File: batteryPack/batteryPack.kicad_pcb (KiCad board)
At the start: 2 copper layers, 212.5 x 83 mm, 38 parts, among them J1 Mirco USB, J10 B1+, J11 B1-, J12 B2-, J13 B1+, J14 B1-, J15 B2+, J16 B2-, J2 B1+, J3 B1-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

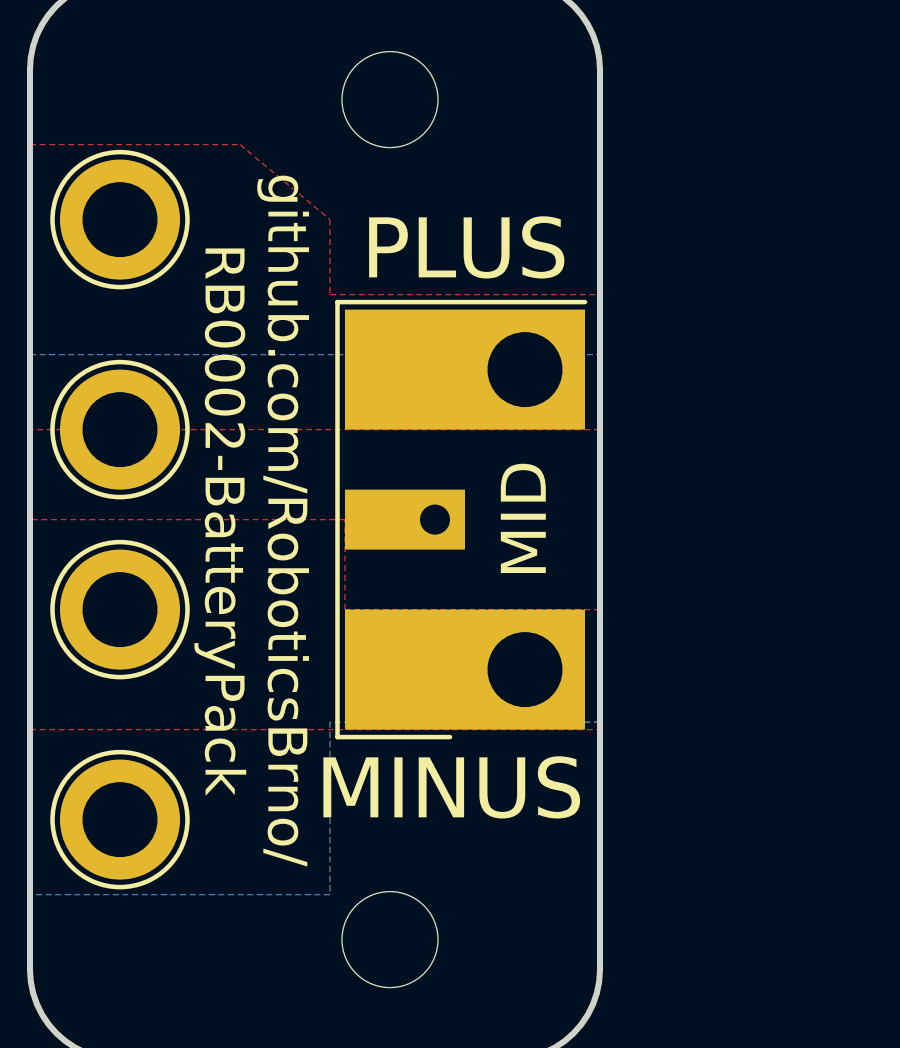
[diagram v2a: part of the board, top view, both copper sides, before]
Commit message: Change connector to screw terminal
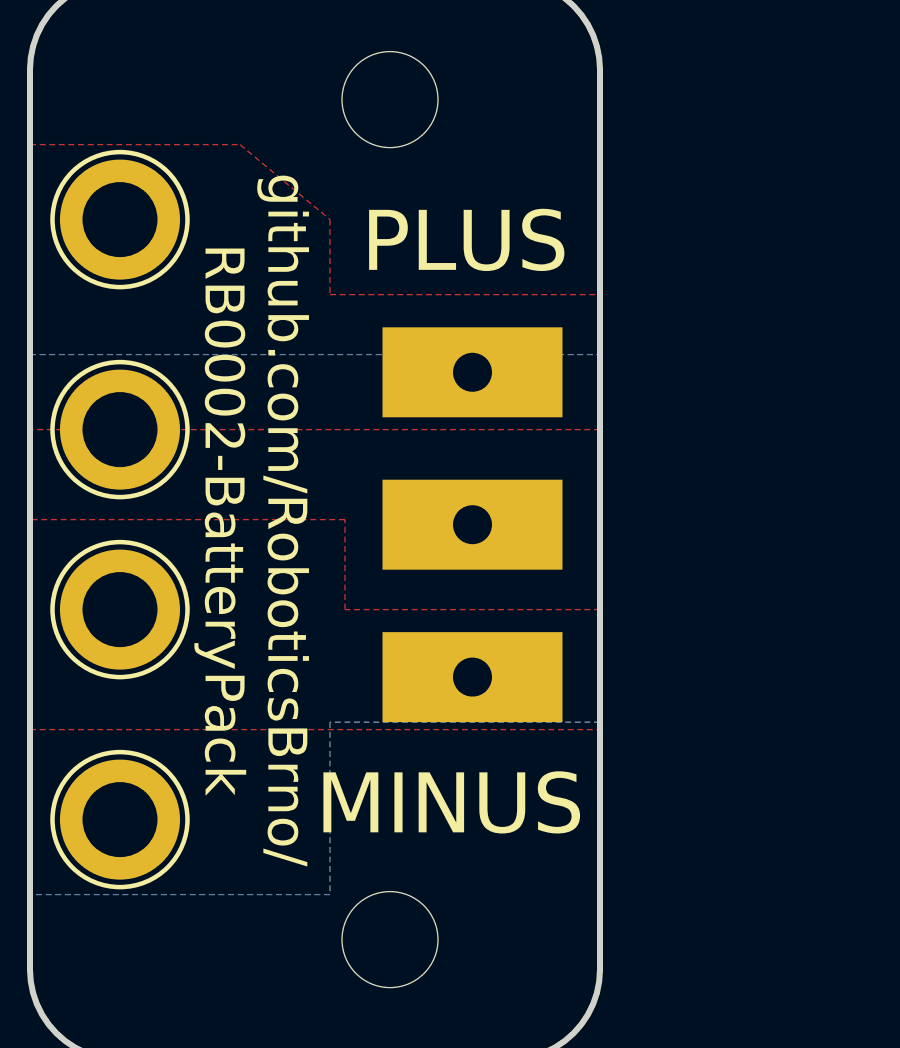
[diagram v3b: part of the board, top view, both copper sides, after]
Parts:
- J6: footprint batteryPack:cableConnector -> batteryPack:Terminal_1x03_P5.08mm_Horizontal
- moved J6 5.53 mm to (131.8, 75.2), turned to 90 degrees
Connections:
- J6 pad 1: /OUT+ -> /OUT-
- J6 pad 3: /OUT- -> /OUT+
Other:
- board text removed: "MID"
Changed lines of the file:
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@@
   (general
     (thickness 1.6)
-    (drawings 131)
+    (drawings 130)
     (tracks 441)
     (zones 0)
@@
   (page A4)
   (layers
-    (0 F.Cu signal hide)
-    (31 B.Cu signal hide)
+    (0 F.Cu signal)
+    (31 B.Cu signal)
     (32 B.Adhes user)
     (33 F.Adhes user)
@@
     (add_net "Net-(D2-Pad2)")
     (add_net "Net-(D3-Pad2)")
+    (add_net "Net-(J1-Pad4)")
     (add_net "Net-(J13-Pad1)")
     (add_net "Net-(J14-Pad1)")
     (add_net "Net-(J15-Pad1)")
     (add_net "Net-(J16-Pad1)")
+    (add_net "Net-(P1-PadA5)")
+    (add_net "Net-(P1-PadA8)")
+    (add_net "Net-(P1-PadB5)")
+    (add_net "Net-(P1-PadB8)")
     (add_net "Net-(R5-Pad1)")
     (add_net "Net-(R6-Pad1)")
     (add_net "Net-(R7-Pad1)")
+    (add_net "Net-(U1-Pad5)")
+    (add_net "Net-(U2-Pad7)")
+    (add_net "Net-(U4-Pad5)")
     (add_net RST)
     (add_net RX)
@@
       (scale (xyz 1 1 1))
       (rotate (xyz -90 0 -90))
+    )
+  )
+  (module batteryPack:Terminal_1x03_P5.08mm_Horizontal (layer F.Cu)
+    (at 131.75 75.25 90)
+    (descr "Terminal Block Phoenix MKDS-3-3-5.08, 3 pins, pitch 5.08mm, size 15.2x11.2mm^2, drill diamater 1.3mm, pad diameter 2.6mm, see http://www.farnell.com/datasheets/2138224.pdf, script-generated using https://github.com/pointhi/kicad-footprint-generator/scripts/TerminalBlock_Phoenix")
+    (tags "THT Terminal Block Phoenix MKDS-3-3-5.08 pitch 5.08mm size 15.2x11.2mm^2 drill 1.3mm pad 2.6mm")
+    (fp_text reference J6 (at 5.08 -6.96 90) (layer F.SilkS) hide
+      (effects (font (size 1 1) (thickness 0.15)))
+    )
+    (fp_text value CableConnector (at 5.08 6.36 90) (layer F.Fab)
+      (effects (font (size 1 1) (thickness 0.15)))
+    )
+    (fp_line (start -2.54 -5.9) (end 12.7 -5.9) (layer F.Fab) (width 0.1))
+    (fp_line (start 12.7 -5.9) (end 12.7 5.3) (layer F.Fab) (width 0.1))
+    (fp_line (start 12.7 5.3) (end -2.04 5.3) (layer F.Fab) (width 0.1))
+    (fp_line (start -2.04 5.3) (end -2.54 4.8) (layer F.Fab) (width 0.1))
+    (fp_line (start -2.54 4.8) (end -2.54 -5.9) (layer F.Fab) (width 0.1))
+    (fp_line (start -2.54 4.8) (end 12.7 4.8) (layer F.Fab) (width 0.1))
+    (fp_line (start -2.54 2.3) (end 12.7 2.3) (layer F.Fab) (width 0.1))
+    (fp_line (start -2.54 -3.9) (end 12.7 -3.9) (layer F.Fab) (width 0.1))
+    (fp_line (start 1.273 -1.517) (end -1.517 1.273) (layer F.Fab) (width 0.1))
+    (fp_line (start -3.04 -6.4) (end -3.04 5.8) (layer F.CrtYd) (width 0.05))
+    (fp_line (start -3.04 5.8) (end 13.21 5.8) (layer F.CrtYd) (width 0.05))
+    (fp_line (start 13.21 5.8) (end 13.21 -6.4) (layer F.CrtYd) (width 0.05))
+    (fp_line (start 13.21 -6.4) (end -3.04 -6.4) (layer F.CrtYd) (width 0.05))
+    (fp_text user %R (at 5.08 3.1 90) (layer F.Fab)
+      (effects (font (size 1 1) (thickness 0.15)))
+    )
+    (pad 1 thru_hole rect (at 0 0 90) (size 3 6) (drill 1.3) (layers *.Cu *.Mask)
+      (net 24 /OUT-))
+    (pad 2 thru_hole rect (at 5.08 0 90) (size 3 6) (drill 1.3) (layers *.Cu *.Mask)
+      (net 23 /MID))
+    (pad 3 thru_hole rect (at 10.16 0 90) (size 3 6) (drill 1.3) (layers *.Cu *.Mask)
+      (net 22 /OUT+))
+    (model ${KISYS3DMOD}/TerminalBlock_Phoenix.3dshapes/TerminalBlock_Phoenix_MKDS-3-3-5.08_1x03_P5.08mm_Horizontal.wrl
+      (at (xyz 0 0 0))
+      (scale (xyz 1 1 1))
+      (rotate (xyz 0 0 0))
     )
   )
@@
       (rotate (xyz 0 0 0))
     )
-  )
-  (module batteryPack:cableConnector (layer F.Cu)
-    (at 133.5 70)
-    (fp_text reference J6 (at 0 -8.5) (layer F.SilkS) hide
-      (effects (font (size 1 1) (thickness 0.15)))
-    )
-    (fp_text value CableConnector (at 0 -11) (layer F.Fab)
-      (effects (font (size 1 1) (thickness 0.15)))
-    )
-    (fp_line (start -6.25 7.25) (end -2.5 7.25) (layer F.SilkS) (width 0.15))
-    (fp_line (start -6.25 -7.25) (end -6.25 7.25) (layer F.SilkS) (width 0.15))
-    (fp_line (start 2 -7.25) (end -6.25 -7.25) (layer F.SilkS) (width 0.15))
-    (pad 2 thru_hole rect (at -3 0) (size 4 2) (drill 1 (offset -1 0)) (layers *.Cu *.Mask)
-      (net 23 /MID))
-    (pad 3 thru_hole rect (at 0 5) (size 8 4) (drill 2.5 (offset -2 0)) (layers *.Cu *.Mask)
-      (net 24 /OUT-))
-    (pad 1 thru_hole rect (at 0 -5) (size 8 4) (drill 2.5 (offset -2 0)) (layers *.Cu *.Mask)
-      (net 22 /OUT+))
   )
   (module batteryPack:2mm_Banana-Vertical (layer F.Cu)
@@
   (gr_arc (start 133 85) (end 133 88) (angle -90) (layer Edge.Cuts) (width 0.2))
   (gr_arc (start 133 55) (end 136 55) (angle -90) (layer Edge.Cuts) (width 0.2))
-  (gr_text MID (at 133.5 70 90) (layer F.SilkS)
-    (effects (font (size 1.5 1.5) (thickness 0.3)))
-  )
-  (gr_text MINUS (at 131 79) (layer F.SilkS)
+  (gr_text MINUS (at 131 79.5) (layer F.SilkS)
     (effects (font (size 2 2) (thickness 0.4)))
   )
-  (gr_text PLUS (at 131.5 61) (layer F.SilkS)
+  (gr_text PLUS (at 131.5 60.75) (layer F.SilkS)
     (effects (font (size 2 2) (thickness 0.4)))
   )

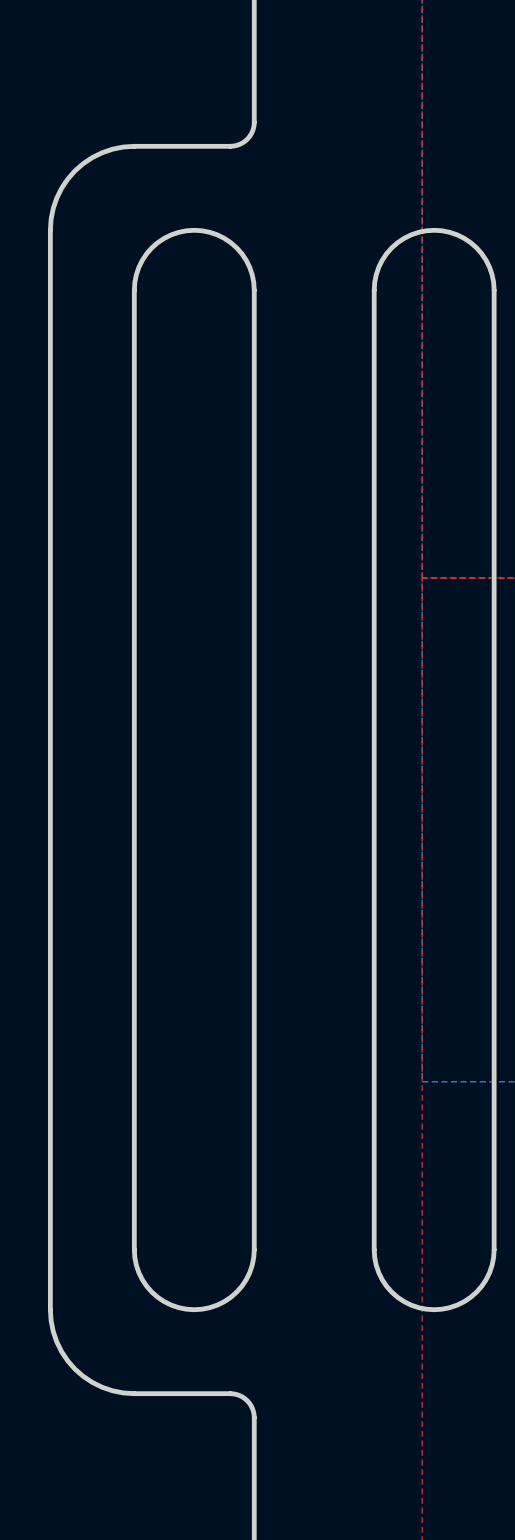
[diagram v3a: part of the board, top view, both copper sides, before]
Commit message: Tune pull handle and battery panel
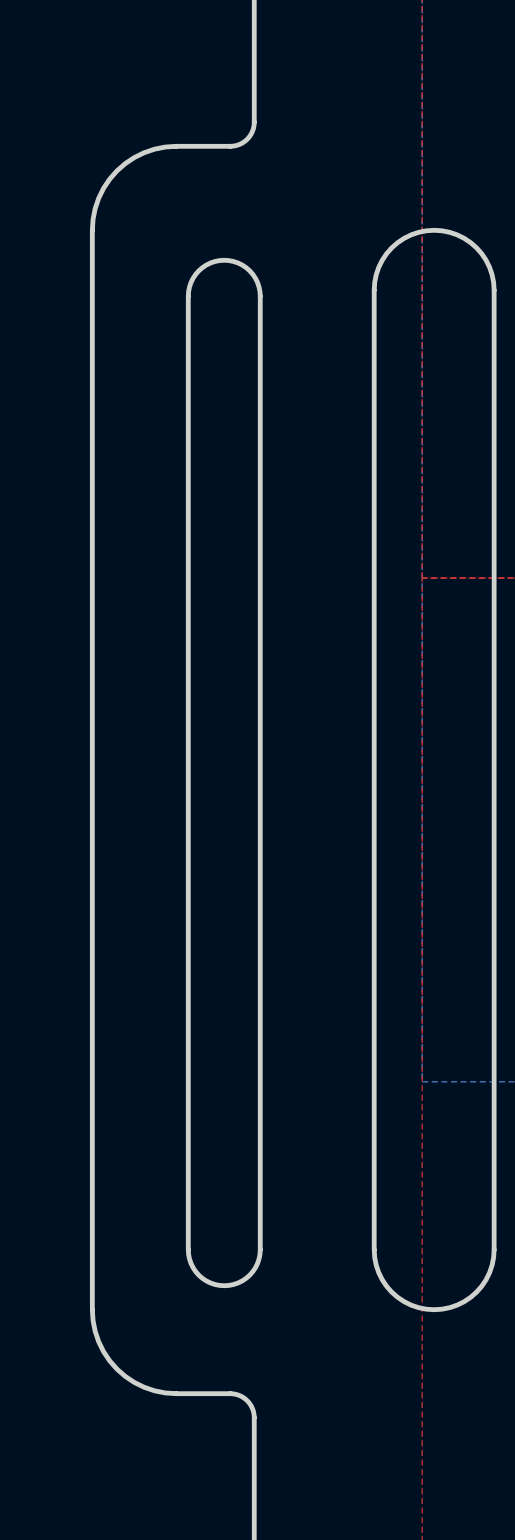
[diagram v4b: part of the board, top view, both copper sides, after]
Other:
- board size 212.5 x 83 mm -> 210.8 x 83 mm
- board text added: "Panel tab position"
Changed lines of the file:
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@@
-(kicad_pcb (version 20171130) (host pcbnew 5.1.5-52549c5~86~ubuntu19.10.1)
+(kicad_pcb (version 20171130) (host pcbnew 5.1.5+dfsg1-2build2)
   (general
     (thickness 1.6)
-    (drawings 130)
+    (drawings 138)
     (tracks 441)
     (zones 0)
@@
     (add_net "Net-(D2-Pad2)")
     (add_net "Net-(D3-Pad2)")
-    (add_net "Net-(J1-Pad4)")
     (add_net "Net-(J13-Pad1)")
     (add_net "Net-(J14-Pad1)")
     (add_net "Net-(J15-Pad1)")
     (add_net "Net-(J16-Pad1)")
-    (add_net "Net-(P1-PadA5)")
-    (add_net "Net-(P1-PadA8)")
-    (add_net "Net-(P1-PadB5)")
-    (add_net "Net-(P1-PadB8)")
     (add_net "Net-(R5-Pad1)")
     (add_net "Net-(R6-Pad1)")
     (add_net "Net-(R7-Pad1)")
-    (add_net "Net-(U1-Pad5)")
-    (add_net "Net-(U2-Pad7)")
-    (add_net "Net-(U4-Pad5)")
     (add_net RST)
     (add_net RX)
@@
   (module batteryPack:BAT_BK-18650-PC4 (layer B.Cu)
     (at 50 70 270)
-    (fp_text reference BT1 (at -36.195 19.05 90) (layer B.SilkS)
+    (fp_text reference BT1 (at -36.195 19.05 90) (layer B.SilkS) hide
       (effects (font (size 1 1) (thickness 0.15)) (justify mirror))
     )
@@
     )
   )
+  (gr_text "Panel tab position" (at 80.5 103) (layer Cmts.User)
+    (effects (font (size 1 1) (thickness 0.15)))
+  )
+  (gr_text "Panel tab position" (at 80.25 86.75) (layer Cmts.User)
+    (effects (font (size 1 1) (thickness 0.15)))
+  )
+  (gr_text "Panel tab position" (at 80.5 53.5) (layer Cmts.User)
+    (effects (font (size 1 1) (thickness 0.15)))
+  )
+  (gr_text "Panel tab position" (at 80.5 37) (layer Cmts.User)
+    (effects (font (size 1 1) (thickness 0.15)))
+  )
+  (gr_line (start 73 37) (end 68.5 37) (layer Cmts.User) (width 0.3))
+  (gr_line (start 73 103) (end 68.5 103) (layer Cmts.User) (width 0.3))
+  (gr_line (start 73 86.75) (end 68.5 86.75) (layer Cmts.User) (width 0.3))
+  (gr_line (start 73 53.5) (end 68.5 53.5) (layer Cmts.User) (width 0.3))
+  (gr_arc (start 28.75 90) (end 27.25 90) (angle -180) (layer Edge.Cuts) (width 0.2))
+  (gr_arc (start 28.75 50.25) (end 30.25 50.25) (angle -180) (layer Edge.Cuts) (width 0.2))
   (gr_line (start 31 109) (end 32.75 109) (layer Edge.Cuts) (width 0.2))
   (gr_line (start 67.25 109) (end 69 109) (layer Edge.Cuts) (width 0.2))
@@
   (gr_arc (start 64.75 29.75) (end 66 29.75) (angle -90) (layer Edge.Cuts) (width 0.2))
   (gr_line (start 64.75 28.5) (end 35.25 28.5) (layer Edge.Cuts) (width 0.2))
-  (gr_line (start 21.5 47.5) (end 21.5 92.5) (layer Edge.Cuts) (width 0.2))
-  (gr_arc (start 25 92.5) (end 21.5 92.5) (angle -90) (layer Edge.Cuts) (width 0.2))
-  (gr_line (start 29 96) (end 25 96) (layer Edge.Cuts) (width 0.2))
-  (gr_arc (start 25 47.5) (end 25 44) (angle -90) (layer Edge.Cuts) (width 0.2))
-  (gr_line (start 29 44) (end 25 44) (layer Edge.Cuts) (width 0.2))
-  (gr_line (start 25 50) (end 25 90) (layer Edge.Cuts) (width 0.2))
-  (gr_arc (start 27.5 50) (end 30 50) (angle -180) (layer Edge.Cuts) (width 0.2))
-  (gr_arc (start 27.5 90) (end 25 90) (angle -180) (layer Edge.Cuts) (width 0.2))
-  (gr_line (start 30 50) (end 30 90) (layer Edge.Cuts) (width 0.2))
+  (gr_line (start 23.25 47.5) (end 23.25 92.5) (layer Edge.Cuts) (width 0.2))
+  (gr_arc (start 26.75 92.5) (end 23.25 92.5) (angle -90) (layer Edge.Cuts) (width 0.2))
+  (gr_line (start 29 96) (end 26.75 96) (layer Edge.Cuts) (width 0.2))
+  (gr_arc (start 26.75 47.5) (end 26.75 44) (angle -90) (layer Edge.Cuts) (width 0.2))
+  (gr_line (start 29 44) (end 26.75 44) (layer Edge.Cuts) (width 0.2))
+  (gr_line (start 27.25 50.25) (end 27.25 90) (layer Edge.Cuts) (width 0.2))
+  (gr_line (start 30.25 50.25) (end 30.25 90) (layer Edge.Cuts) (width 0.2))
   (gr_arc (start 29 97) (end 30 97) (angle -90) (layer Edge.Cuts) (width 0.2))
   (gr_line (start 30 97) (end 30 108) (layer Edge.Cuts) (width 0.2))
@@
   (gr_line (start 122.25 48.75) (end 122.25 90) (layer F.CrtYd) (width 0.15))
   (dimension 40 (width 0.3) (layer F.Fab)
-    (gr_text "40,000 mm" (at 50 118.449999) (layer F.Fab)
-      (effects (font (size 1 1) (thickness 0.15)))
-    )
-    (feature1 (pts (xy 70 108) (xy 70 117.58642)))
-    (feature2 (pts (xy 30 108) (xy 30 117.58642)))
-    (crossbar (pts (xy 30 116.999999) (xy 70 116.999999)))
-    (arrow1a (pts (xy 70 116.999999) (xy 68.873496 117.58642)))
-    (arrow1b (pts (xy 70 116.999999) (xy 68.873496 116.413578)))
-    (arrow2a (pts (xy 30 116.999999) (xy 31.126504 117.58642)))
-    (arrow2b (pts (xy 30 116.999999) (xy 31.126504 116.413578)))
+    (gr_text "40,000 mm" (at 50 121.2) (layer F.Fab)
+      (effects (font (size 1 1) (thickness 0.15)))
+    )
+    (feature1 (pts (xy 70 108) (xy 70 120.336421)))
+    (feature2 (pts (xy 30 108) (xy 30 120.336421)))
+    (crossbar (pts (xy 30 119.75) (xy 70 119.75)))
+    (arrow1a (pts (xy 70 119.75) (xy 68.873496 120.336421)))
+    (arrow1b (pts (xy 70 119.75) (xy 68.873496 119.163579)))
+    (arrow2a (pts (xy 30 119.75) (xy 31.126504 120.336421)))
+    (arrow2b (pts (xy 30 119.75) (xy 31.126504 119.163579)))
   )
   (dimension 78 (width 0.3) (layer F.Fab)
@@
   (gr_line (start 15 70) (end 280 70) (layer Eco1.User) (width 0.15))
   (gr_line (start 170 15) (end 170 195) (layer Eco1.User) (width 1))
-  (gr_text "Battery Connector\n" (at 130 20) (layer Eco1.User)
+  (gr_text "Battery Connector\n" (at 130 17.25) (layer Eco1.User)
     (effects (font (size 5 5) (thickness 0.5)))
   )
-  (gr_text "Battery Pack" (at 50 20) (layer Eco1.User)
+  (gr_text "Battery Pack" (at 50 16.25) (layer Eco1.User)
     (effects (font (size 5 5) (thickness 0.5)))
   )
